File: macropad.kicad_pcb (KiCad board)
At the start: 2 copper layers, 125.5 x 56 mm, 7 parts, among them SW1 SW_Push, SW2 SW_Push, SW3 SW_Push, SW4 SW_Push, SW5 SW_Push, SW6 SW_Push

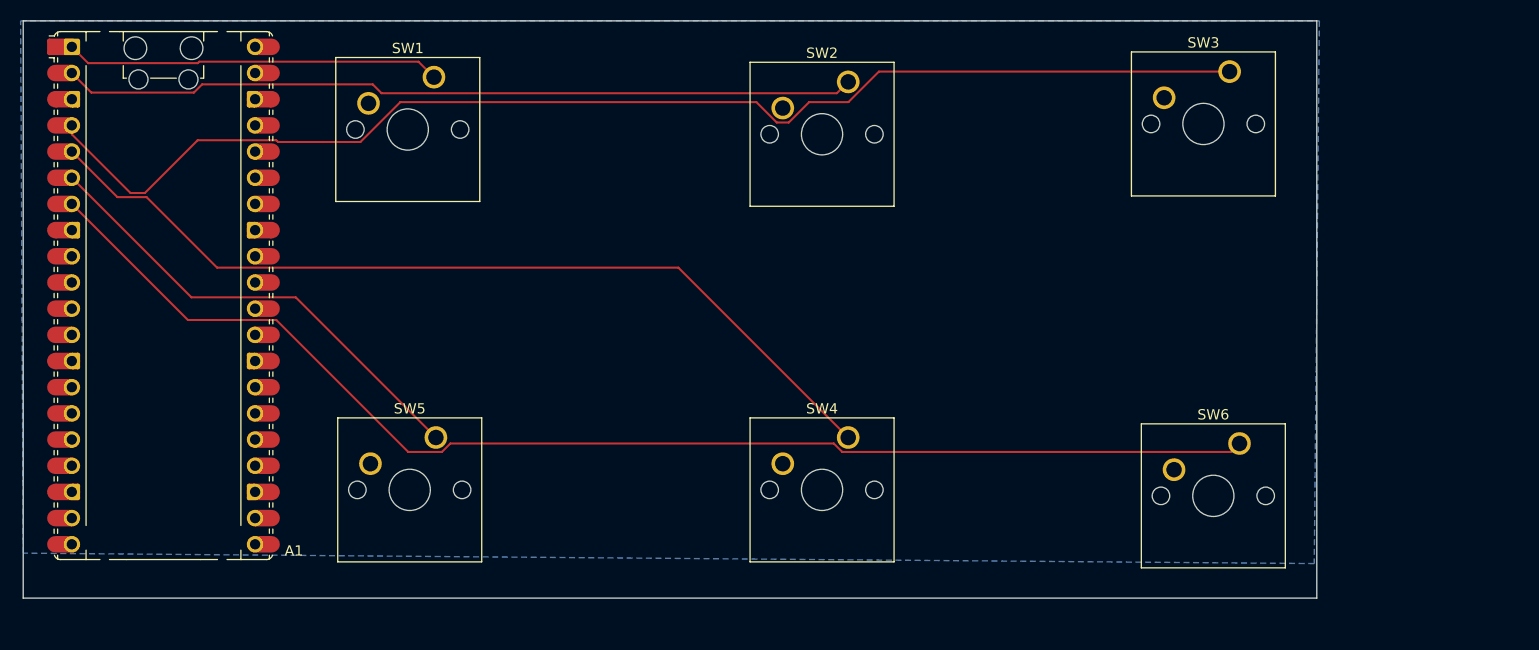
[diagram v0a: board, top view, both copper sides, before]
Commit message: Added 12 more switches yesss
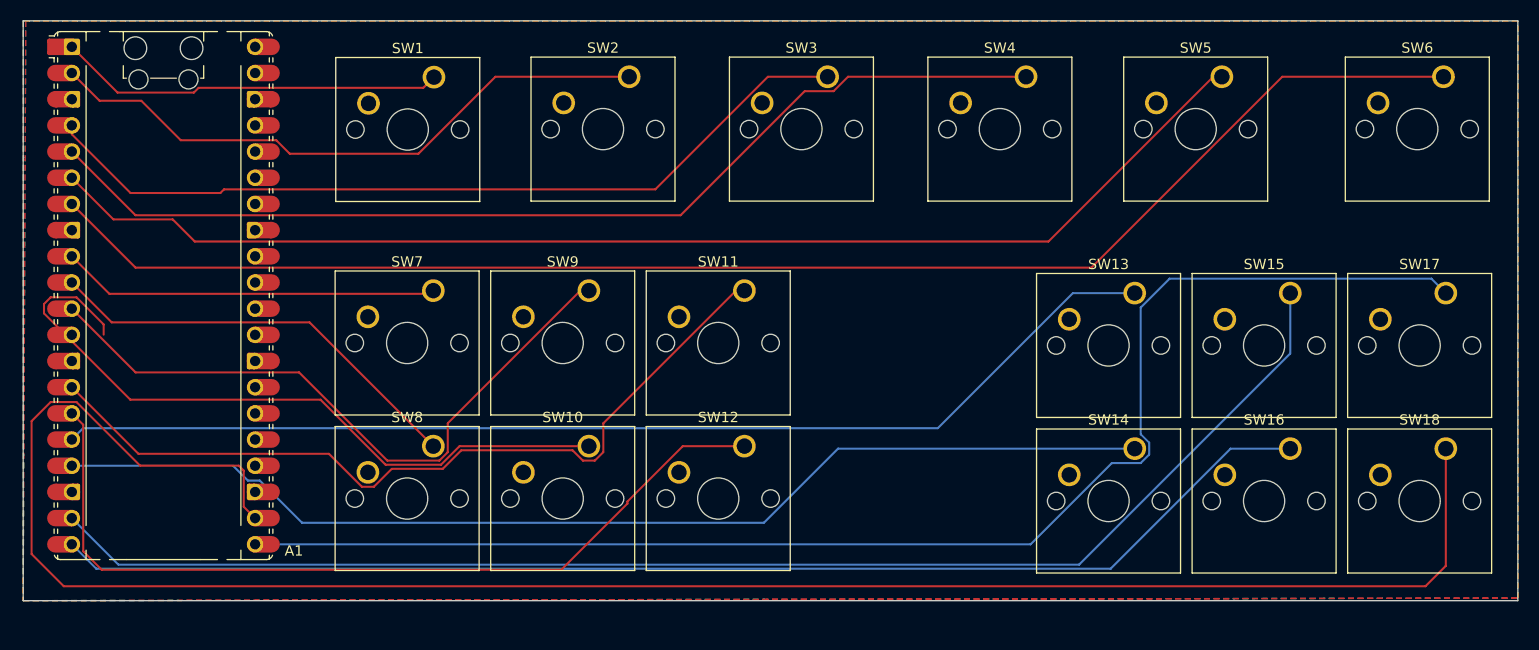
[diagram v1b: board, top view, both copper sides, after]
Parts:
- added SW10: SW_Push, Button_Switch_Keyboard:SW_Cherry_MX_1.00u_PCB, F.Cu at (64.9, 51.3)
- added SW11: SW_Push, Button_Switch_Keyboard:SW_Cherry_MX_1.00u_PCB, F.Cu at (80.0, 36.2)
- added SW12: SW_Push, Button_Switch_Keyboard:SW_Cherry_MX_1.00u_PCB, F.Cu at (80.0, 51.3)
- added SW13: SW_Push, Button_Switch_Keyboard:SW_Cherry_MX_1.00u_PCB, F.Cu at (117.8, 36.4)
- added SW14: SW_Push, Button_Switch_Keyboard:SW_Cherry_MX_1.00u_PCB, F.Cu at (117.8, 51.5)
- added SW15: SW_Push, Button_Switch_Keyboard:SW_Cherry_MX_1.00u_PCB, F.Cu at (132.9, 36.4)
- added SW16: SW_Push, Button_Switch_Keyboard:SW_Cherry_MX_1.00u_PCB, F.Cu at (132.9, 51.5)
- added SW17: SW_Push, Button_Switch_Keyboard:SW_Cherry_MX_1.00u_PCB, F.Cu at (148.0, 36.4)
- added SW18: SW_Push, Button_Switch_Keyboard:SW_Cherry_MX_1.00u_PCB, F.Cu at (148.0, 51.5)
- added SW7: SW_Push, Button_Switch_Keyboard:SW_Cherry_MX_1.00u_PCB, F.Cu at (49.8, 36.2)
- added SW8: SW_Push, Button_Switch_Keyboard:SW_Cherry_MX_1.00u_PCB, F.Cu at (49.8, 51.3)
- added SW9: SW_Push, Button_Switch_Keyboard:SW_Cherry_MX_1.00u_PCB, F.Cu at (64.9, 36.2)
- moved SW5 83.9 mm to (126.3, 15.4)
- moved SW6 40.7 mm to (147.8, 15.4)
- moved SW4 39.0 mm to (107.3, 15.4)
- moved SW3 39.0 mm to (88.0, 15.4)
- moved SW2 21.3 mm to (68.8, 15.4)
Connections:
- A1 pad 10: unconnected-(A1-GPIO7-Pad10)_1 -> /s8g
- A1 pad 11: unconnected-(A1-GPIO8-Pad11) -> /s9g
- A1 pad 12: unconnected-(A1-GPIO9-Pad12)_1 -> /s10g
- A1 pad 14: unconnected-(A1-GPIO10-Pad14)_1 -> /s11g
- A1 pad 15: unconnected-(A1-GPIO11-Pad15)_1 -> /s12g
- A1 pad 16: unconnected-(A1-GPIO12-Pad16) -> /s13g
- A1 pad 17: unconnected-(A1-GPIO13-Pad17) -> /s14g
- A1 pad 19: unconnected-(A1-GPIO14-Pad19) -> /s15g
- A1 pad 20: unconnected-(A1-GPIO15-Pad20) -> /s16g
- A1 pad 21: unconnected-(A1-GPIO16-Pad21)_1 -> /s17g
- A1 pad 22: unconnected-(A1-GPIO17-Pad22) -> /s18g
- A1 pad 9: unconnected-(A1-GPIO6-Pad9)_1 -> /s7g
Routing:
- net /s18g: track 0.00 -> 192.8 mm
- net /s17g: track 0.00 -> 136.3 mm
- net /s15g: track 0.00 -> 134.4 mm
- net /s16g: track 0.00 -> 124.0 mm
- net /s13g: track 0.00 -> 109.0 mm
- net /s14g: track 0.00 -> 108.4 mm
- net /s12g: track 0.00 -> 83.8 mm
- net /s11g: track 0.00 -> 79.6 mm
- net /s5g: track 45.8 -> 120.8 mm
- net /s10g: track 0.00 -> 68.7 mm
- net /s9g: track 0.00 -> 64.7 mm
- net /s8g: track 0.00 -> 41.6 mm
- net /s3g: track 122.2 -> 81.2 mm
- net /s7g: track 0.00 -> 36.7 mm
- net /s6g: track 124.3 -> 143.3 mm
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- added copper zone on F.Cu, net GND
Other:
- board size 125.5 x 56 mm -> 145 x 56.2 mm

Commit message: Gerber and drill files made!
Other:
- board text added: "Email me@kushjoshi.me for help!"
- board text added: "Kush's Cool Macropad Project"
- board text added: "kushjoshi.me"
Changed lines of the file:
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@@
 		(layer "Edge.Cuts")
+	)
+	(gr_text "Email me@kushjoshi.me for help!"
+		(at 89.5 42.75 0)
+		(layer "F.SilkS")
+		(effects
+			(font
+				(size 0.5 0.5)
+				(thickness 0.1)
+			)
+			(justify left bottom)
+		)
+	)
+	(gr_text "Kush's Cool Macropad Project"
+		(at 90 39.5 0)
+		(layer "F.SilkS")
+		(effects
+			(font
+				(size 0.5 0.5)
+				(thickness 0.1)
+			)
+			(justify left bottom)
+		)
+	)
+	(gr_text "kushjoshi.me\n"
+		(at 90.75 41.5 0)
+		(layer "F.SilkS")
+		(effects
+			(font
+				(size 1 1)
+				(thickness 0.1)
+			)
+			(justify left bottom)
+		)
 	)
 	(segment

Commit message: I made the silkscreen better, before it would have came from the factory completely messed up, however now it should work, I also just updated the Gerbers
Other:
- board text added: "Kush's Macropad"
- board text added: "me@kushjoshi.me"
- board text removed: "Email me@kushjoshi.me for help!"
- board text removed: "Kush's Cool Macropad Project"
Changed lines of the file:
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@@
 			(outputformat 1)
 			(mirror no)
-			(drillshape 1)
+			(drillshape 0)
 			(scaleselection 1)
-			(outputdirectory "")
+			(outputdirectory "Gerbers/")
 		)
 	)
@@
 		(layer "Edge.Cuts")
 	)
-	(gr_text "Email me@kushjoshi.me for help!"
-		(at 89.5 42.75 0)
+	(gr_text "me@kushjoshi.me"
+		(at 91.25 39.25 0)
 		(layer "F.SilkS")
 		(effects
 			(font
-				(size 0.5 0.5)
-				(thickness 0.1)
+				(size 0.85 0.85)
+				(thickness 0.15)
+				(bold yes)
 			)
 			(justify left bottom)
 		)
 	)
-	(gr_text "Kush's Cool Macropad Project"
-		(at 90 39.5 0)
+	(gr_text "Kush's Macropad"
+		(at 90 36.25 0)
 		(layer "F.SilkS")
 		(effects
 			(font
-				(size 0.5 0.5)
-				(thickness 0.1)
+				(size 1 1)
+				(thickness 0.15)
 			)
 			(justify left bottom)
@@
 	)
 	(gr_text "kushjoshi.me\n"
-		(at 90.75 41.5 0)
+		(at 92.25 37.75 0)
 		(layer "F.SilkS")
 		(effects
 			(font
 				(size 1 1)
-				(thickness 0.1)
+				(thickness 0.15)
 			)
 			(justify left bottom)
@@
 	)
 	(segment
+		(start 148.015 51.5)
+		(end 148.015 62.872944)
+		(width 0.2)
+		(layer "F.Cu")
+		(net "/s18g")
+	)
+	(segment
+		(start 30.917108 53.15)
+		(end 31.395 53.627892)
+		(width 0.2)
+		(layer "F.Cu")
+		(net "/s18g")
+	)
+	(segment
+		(start 148.015 62.872944)
+		(end 146.037944 64.85)
+		(width 0.2)
+		(layer "F.Cu")
+		(net "/s18g")
+	)
+	(segment
+		(start 21.345635 53.15)
+		(end 30.917108 53.15)
+		(width 0.2)
+		(layer "F.Cu")
+		(net "/s18g")
+	)
+	(segment
+		(start 10.815 48.829364)
+		(end 12.664364 46.98)
+		(width 0.2)
+		(layer "F.Cu")
+		(net "/s18g")
+	)
+	(segment
+		(start 31.395 57.135)
+		(end 32.5 58.24)
+		(width 0.2)
+		(layer "F.Cu")
+		(net "/s18g")
+	)
+	(segment
+		(start 15.175635 46.98)
+		(end 21.345635 53.15)
+		(width 0.2)
+		(layer "F.Cu")
+		(net "/s18g")
+	)
+	(segment
+		(start 31.395 53.627892)
+		(end 31.395 57.135)
+		(width 0.2)
+		(layer "F.Cu")
+		(net "/s18g")
+	)
+	(segment
+		(start 13.937306 64.85)
+		(end 10.815 61.727691)
+		(width 0.2)
+		(layer "F.Cu")
+		(net "/s18g")
+	)
+	(segment
+		(start 10.815 61.727691)
+		(end 10.815 48.829364)
+		(width 0.2)
+		(layer "F.Cu")
+		(net "/s18g")
+	)
+	(segment
+		(start 12.664364 46.98)
+		(end 15.175635 46.98)
+		(width 0.2)
+		(layer "F.Cu")
+		(net "/s18g")
+	)
+	(segment
+		(start 146.037944 64.85)
+		(end 13.937306 64.85)
+		(width 0.2)
+		(layer "F.Cu")
+		(net "/s18g")
+	)
+	(segment
+		(start 127.135101 51.5)
+		(end 123.5 55.135101)
+		(width 0.2)
+		(layer "B.Cu")
+		(net "/s16g")
+	)
+	(segment
+		(start 123.5 55.152056)
+		(end 115.502056 63.15)
+		(width 0.2)
+		(layer "B.Cu")
+		(net "/s16g")
+	)
+	(segment
+		(start 123.5 55.135101)
+		(end 123.5 55.152056)
+		(width 0.2)
+		(layer "B.Cu")
+		(net "/s16g")
+	)
+	(segment
+		(start 115.502056 63.15)
+		(end 17.09 63.15)
+		(width 0.2)
+		(layer "B.Cu")
+		(net "/s16g")
+	)
+	(segment
+		(start 132.925 51.5)
+		(end 127.135101 51.5)
+		(width 0.2)
+		(layer "B.Cu")
+		(net "/s16g")
+	)
+	(segment
+		(start 17.09 63.15)
+		(end 14.72 60.78)
+		(width 0.2)
+		(layer "B.Cu")
+		(net "/s16g")
+	)
+	(segment
+		(start 111.84 36.41)
+		(end 98.73 49.52)
+		(width 0.2)
+		(layer "B.Cu")
+		(net "/s13g")
+	)
+	(segment
+		(start 117.835 36.41)
+		(end 111.84 36.41)
+		(width 0.2)
+		(layer "B.Cu")
+		(net "/s13g")
+	)
+	(segment
+		(start 15.82 49.52)
+		(end 14.72 50.62)
+		(width 0.2)
+		(layer "B.Cu")
+		(net "/s13g")
+	)
+	(segment
+		(start 98.73 49.52)
+		(end 15.82 49.52)
+		(width 0.2)
+		(layer "B.Cu")
+		(net "/s13g")
+	)
+	(segment
 		(start 19.155 16.955)
 		(end 14.72 12.52)
@@
 	)
 	(segment
-		(start 148.015 51.5)
-		(end 148.015 62.872944)
-		(width 0.2)
-		(layer "F.Cu")
-		(net "/s18g")
-	)
-	(segment
-		(start 30.917108 53.15)
-		(end 31.395 53.627892)
-		(width 0.2)
-		(layer "F.Cu")
-		(net "/s18g")
-	)
-	(segment
-		(start 148.015 62.872944)
-		(end 146.037944 64.85)
-		(width 0.2)
-		(layer "F.Cu")
-		(net "/s18g")
-	)
-	(segment
-		(start 21.345635 53.15)
-		(end 30.917108 53.15)
-		(width 0.2)
-		(layer "F.Cu")
-		(net "/s18g")
-	)
-	(segment
-		(start 10.815 48.829364)
-		(end 12.664364 46.98)
-		(width 0.2)
-		(layer "F.Cu")
-		(net "/s18g")
-	)
-	(segment
-		(start 31.395 57.135)
-		(end 32.5 58.24)
-		(width 0.2)
-		(layer "F.Cu")
-		(net "/s18g")
-	)
-	(segment
-		(start 15.175635 46.98)
-		(end 21.345635 53.15)
-		(width 0.2)
-		(layer "F.Cu")
-		(net "/s18g")
-	)
-	(segment
-		(start 31.395 53.627892)
-		(end 31.395 57.135)
-		(width 0.2)
-		(layer "F.Cu")
-		(net "/s18g")
-	)
-	(segment
-		(start 13.937306 64.85)
-		(end 10.815 61.727691)
-		(width 0.2)
-		(layer "F.Cu")
-		(net "/s18g")
-	)
-	(segment
-		(start 10.815 61.727691)
-		(end 10.815 48.829364)
-		(width 0.2)
-		(layer "F.Cu")
-		(net "/s18g")
-	)
-	(segment
-		(start 12.664364 46.98)
-		(end 15.175635 46.98)
-		(width 0.2)
-		(layer "F.Cu")
-		(net "/s18g")
-	)
-	(segment
-		(start 146.037944 64.85)
-		(end 13.937306 64.85)
-		(width 0.2)
-		(layer "F.Cu")
-		(net "/s18g")
-	)
-	(segment
 		(start 37.052708 58.69)
 		(end 32.957708 54.595)
@@
 	)
 	(segment
+		(start 132.925 36.41)
+		(end 132.925 42.273402)
+		(width 0.2)
+		(layer "B.Cu")
+		(net "/s15g")
+	)
+	(segment
+		(start 132.925 42.273402)
+		(end 112.448402 62.75)
+		(width 0.2)
+		(layer "B.Cu")
+		(net "/s15g")
+	)
+	(segment
+		(start 112.448402 62.75)
+		(end 19.23 62.75)
+		(width 0.2)
+		(layer "B.Cu")
+		(net "/s15g")
+	)
+	(segment
+		(start 19.23 62.75)
+		(end 14.72 58.24)
+		(width 0.2)
+		(layer "B.Cu")
+		(net "/s15g")
+	)
+	(segment
 		(start 118.414899 37.81)
 		(end 118.414899 50.1)
@@
 		(net "/s17g")
 	)
-	(segment
-		(start 132.925 36.41)
-		(end 132.925 42.273402)
-		(width 0.2)
-		(layer "B.Cu")
-		(net "/s15g")
-	)
-	(segment
-		(start 132.925 42.273402)
-		(end 112.448402 62.75)
-		(width 0.2)
-		(layer "B.Cu")
-		(net "/s15g")
-	)
-	(segment
-		(start 112.448402 62.75)
-		(end 19.23 62.75)
-		(width 0.2)
-		(layer "B.Cu")
-		(net "/s15g")
-	)
-	(segment
-		(start 19.23 62.75)
-		(end 14.72 58.24)
-		(width 0.2)
-		(layer "B.Cu")
-		(net "/s15g")
-	)
-	(segment
-		(start 111.84 36.41)
-		(end 98.73 49.52)
-		(width 0.2)
-		(layer "B.Cu")
-		(net "/s13g")
-	)
-	(segment
-		(start 117.835 36.41)
-		(end 111.84 36.41)
-		(width 0.2)
-		(layer "B.Cu")
-		(net "/s13g")
-	)
-	(segment
-		(start 15.82 49.52)
-		(end 14.72 50.62)
-		(width 0.2)
-		(layer "B.Cu")
-		(net "/s13g")
-	)
-	(segment
-		(start 98.73 49.52)
-		(end 15.82 49.52)
-		(width 0.2)
-		(layer "B.Cu")
-		(net "/s13g")
-	)
-	(segment
-		(start 127.135101 51.5)
-		(end 123.5 55.135101)
-		(width 0.2)
-		(layer "B.Cu")
-		(net "/s16g")
-	)
-	(segment
-		(start 123.5 55.152056)
-		(end 115.502056 63.15)
-		(width 0.2)
-		(layer "B.Cu")
-		(net "/s16g")
-	)
-	(segment
-		(start 123.5 55.135101)
-		(end 123.5 55.152056)
-		(width 0.2)
-		(layer "B.Cu")
-		(net "/s16g")
-	)
-	(segment
-		(start 115.502056 63.15)
-		(end 17.09 63.15)
-		(width 0.2)
-		(layer "B.Cu")
-		(net "/s16g")
-	)
-	(segment
-		(start 132.925 51.5)
-		(end 127.135101 51.5)
-		(width 0.2)
-		(layer "B.Cu")
-		(net "/s16g")
-	)
-	(segment
-		(start 17.09 63.15)
-		(end 14.72 60.78)
-		(width 0.2)
-		(layer "B.Cu")
-		(net "/s16g")
-	)
 	(zone

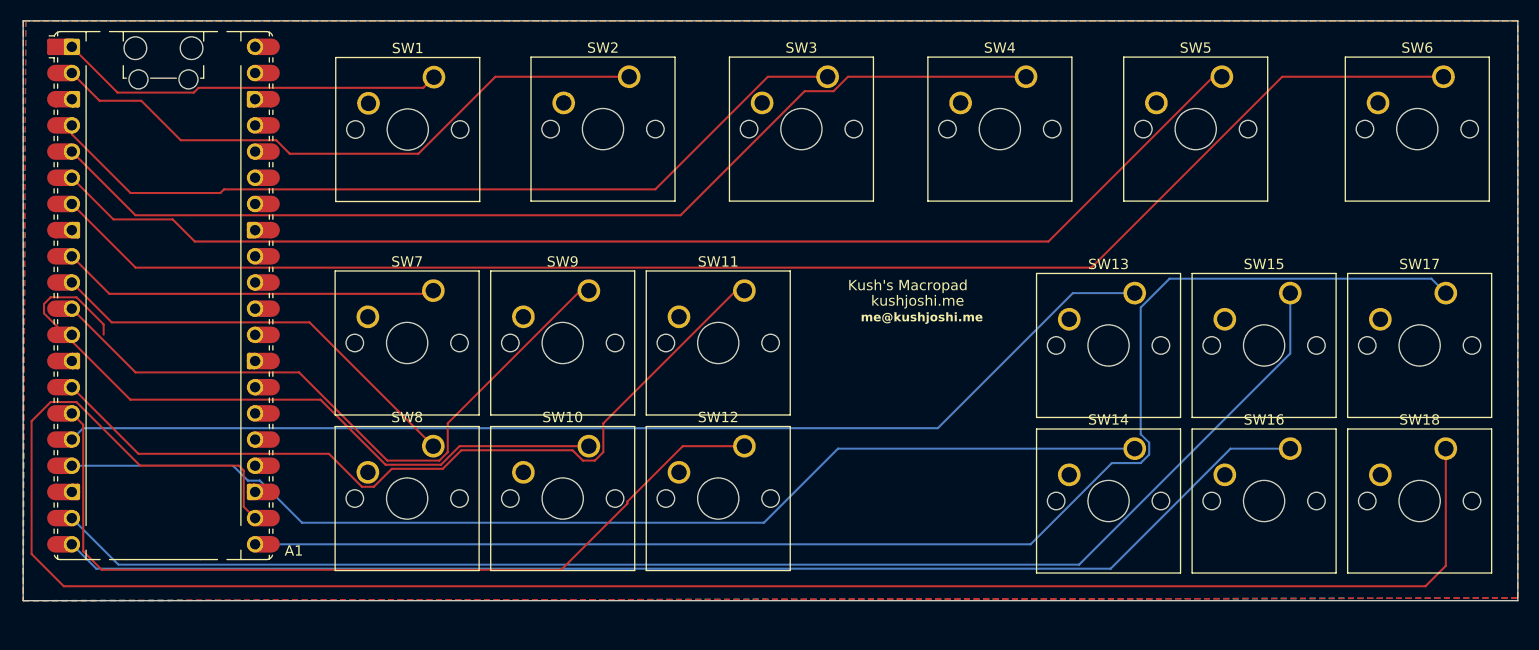
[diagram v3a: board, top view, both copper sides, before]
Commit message: Re-spaced all switches into a proper grid so it is properly manufacturable. I had to reroute, and I have updated the Gerbers and plate.stl files.
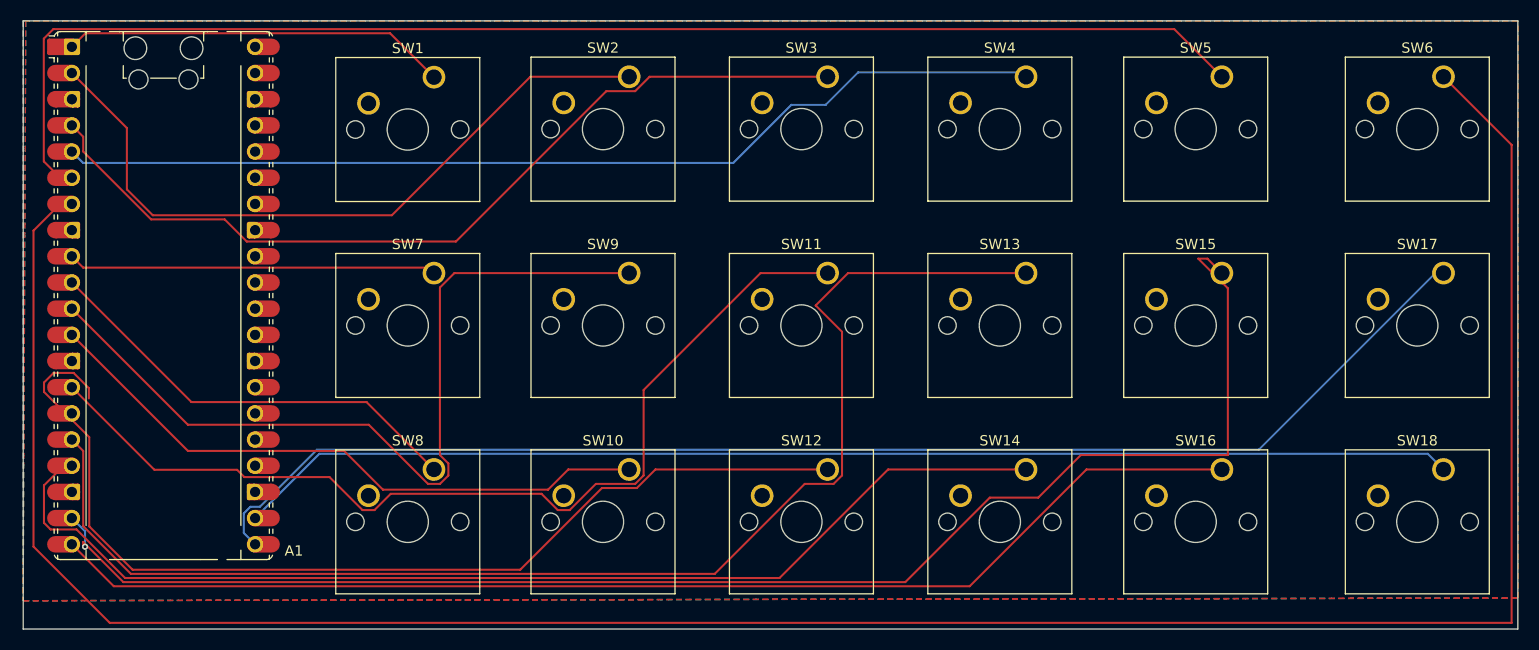
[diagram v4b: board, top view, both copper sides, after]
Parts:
- moved SW14 10.7 mm to (107.3, 53.5)
- moved SW13 10.7 mm to (107.3, 34.5)
- moved SW12 8.38 mm to (88.0, 53.5)
- moved SW11 8.25 mm to (88.0, 34.5)
- moved SW16 6.94 mm to (126.3, 53.5)
- moved SW15 6.91 mm to (126.3, 34.5)
- moved SW10 4.52 mm to (68.8, 53.5)
- moved SW9 4.26 mm to (68.8, 34.5)
- moved SW8 2.26 mm to (49.9, 53.5)
- moved SW18 2.03 mm to (147.8, 53.5)
- moved SW17 1.95 mm to (147.8, 34.5)
- moved SW7 1.70 mm to (49.9, 34.5)
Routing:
- net /s6g: track 143.3 -> 237.6 mm
- net /s18g: track 192.8 -> 118.5 mm
- net /s13g: track 109.0 -> 127.6 mm
- net /s9g: track 64.7 -> 81.4 mm
- net /s12g: track 83.8 -> 99.5 mm
- net /s11g: track 79.6 -> 93.9 mm
- net /s5g: track 120.8 -> 131.9 mm
- net /s15g: track 134.4 -> 144.7 mm, vias 0 -> 1
- net /s2g: track 60.4 -> 68.8 mm
- net /s10g: track 68.7 -> 61.1 mm
- net /s17g: track 136.3 -> 129.5 mm
- net /s16g: track 124.0 -> 117.9 mm
- net /s3g: track 81.2 -> 85.4 mm
- net /s4g: track 100.7 -> 98.3 mm
- net /s8g: track 41.6 -> 42.6 mm
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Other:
- board size 145 x 56.2 mm -> 145 x 59 mm
